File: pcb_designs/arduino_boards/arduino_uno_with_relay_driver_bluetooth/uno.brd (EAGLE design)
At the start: 96.2 x 69.8 mm, 27 parts, among them IC1 ATMEGA328, IC2 7805, Q1 12MHZ

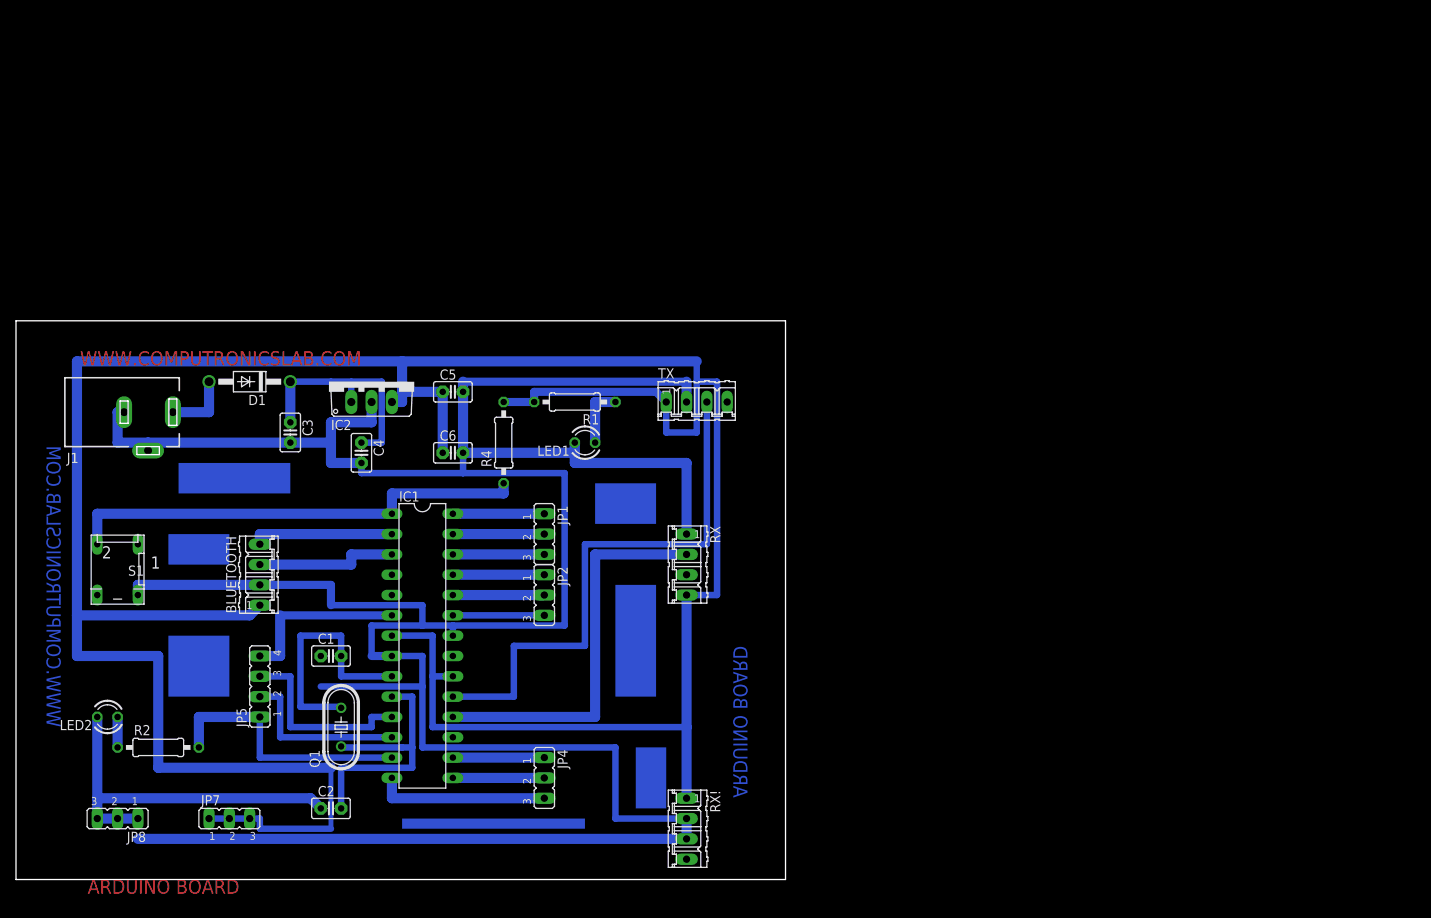
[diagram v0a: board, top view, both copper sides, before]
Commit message: 
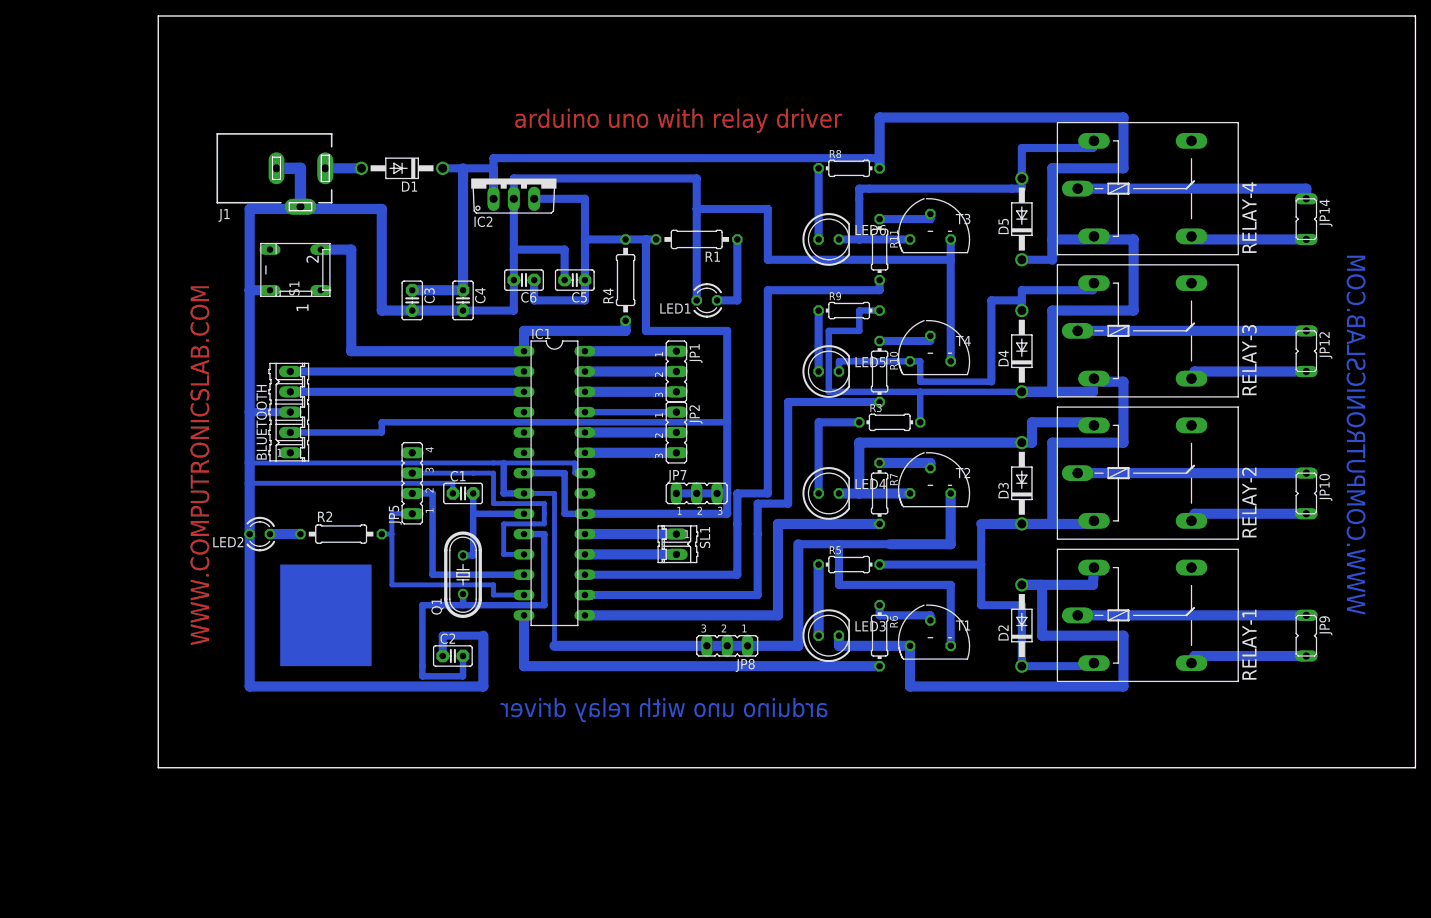
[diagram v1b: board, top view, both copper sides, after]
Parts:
- removed JP4: (no value), jumper:JP2
- removed RX, RX!, TX: (no value), con-amp-quick:04P
- added D2, D3, D4, D5: 1N4007, diode:DO41-10
- added JP10, JP12, JP14, JP9: AC CONNECTOR, jumper:JP1
- added LED3, LED4, LED5, LED6: 5MM, led:LED5MM
- added R10, R11, R6, R7: 5.6K, rcl:0204/7
- added R3, R5, R8, R9: 1K, rcl:0204/7
- added RELAY-1, RELAY-2, RELAY-3, RELAY-4: 12V, relay:G5LE
- added SL1: (no value), con-amp-quick:02P
- added T1, T2, T3, T4: BC547, transistor:TO92
- BLUETOOTH: value (none) -> 5 pin; device con-amp-quick:04P -> con-amp-quick:05P
- C3: value 470UF -> 100UF
- moved JP8 79.2 mm to (74.9, 24.1)
- moved JP7 71.2 mm to (71.1, 43.2)
- moved S1 43.3 mm to (21.6, 71.1), turned to 90 degrees
- moved J1 35.9 mm to (21.6, 83.8)
- moved R2 35.1 mm to (26.7, 38.1)
- moved D1 32.8 mm to (34.3, 83.8)
- moved JP5 31.8 mm to (35.6, 44.5)
- moved IC2 31.0 mm to (48.3, 82.5)
- moved LED2 29.8 mm to (16.5, 38.1)
- moved IC1 26.2 mm to (53.3, 44.5)
- moved C1 26.2 mm to (41.9, 43.2)
- moved JP1 26.2 mm to (68.6, 58.4)
- moved JP2 26.2 mm to (68.6, 50.8)
- moved R1 25.4 mm to (71.1, 74.9)
- moved R4 25.4 mm to (62.2, 69.8)
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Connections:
- removed net N$17: BLUETOOTH.3, IC1.3
- removed net N$18: IC1.6, JP5.4
- removed net N$22: IC1.14, JP4.3
- removed net N$23: IC1.15, JP4.2
- removed net N$24: IC1.16, JP4.1
- removed net N$26: IC1.18, RX.2
- new net N$16: BLUETOOTH.4, IC1.3
- new net N$28: D2.A, LED3.K, RELAY-1.2, T1.3
- new net N$29: R7.1, T2.2
- new net N$30: R6.1, T1.2
- new net N$33: LED3.A, R5.1
- new net N$34: LED4.A, R3.1
- new net N$35: JP9.2, RELAY-1.S
- new net N$36: JP9.1, RELAY-1.P
- new net N$38: JP10.2, RELAY-2.S
- new net N$39: JP10.1, RELAY-2.P
- new net N$41: IC1.14, R6.2
- new net N$42: D3.A, LED4.K, RELAY-2.2, T2.3
- new net N$43: D4.A, LED5.K, RELAY-3.2, T4.3
- new net N$45: R11.1, T3.2
- new net N$46: R10.1, T4.2
- new net N$47: LED5.A, R9.1
- new net N$48: LED6.A, R8.1
- new net N$49: JP12.2, RELAY-3.S
- new net N$50: JP12.1, RELAY-3.P
- new net N$51: JP14.2, RELAY-4.S
- new net N$53: JP14.1, RELAY-4.P
- new net N$55: BLUETOOTH.3, C1.1, C2.1, C3.2, C4.2, C5.2, C6.2, IC1.22, IC1.8, IC2.2, J1.2, J1.3, JP8.1, JP8.2, JP8.3, LED1.K, LED2.K, S1.4, T1.1, T2.1, T3.1, T4.1
- new net N$56: IC1.16, R10.2
- new net N$57: IC1.17, R11.2
- new net N$58: D5.A, LED6.K, RELAY-4.2, T3.3
- new net N$59: IC1.15, R7.2
- net N$14: now also JP5.4; no longer BLUETOOTH.4, IC1.2
- net N$15: now also BLUETOOTH.5, IC1.2; no longer S1.3
- net N$27: now also SL1.1; no longer TX.3
- net N$4: now also BLUETOOTH.2; no longer BLUETOOTH.1, RX!.1, RX.4, TX.1
- net N$5: now also IC1.18, SL1.2; no longer BLUETOOTH.2, C1.1, C2.1, C3.2, C4.2, C5.2, C6.2, IC1.22, IC1.8, IC2.2, J1.2, J1.3, JP8.1, JP8.2, JP8.3, LED1.K, LED2.K, RX!.2, RX!.3, RX.1, S1.4, TX.2
- net N$7: now also D2.C, D3.C, D4.C, D5.C, R3.2, R5.2, R8.2, R9.2, RELAY-1.1, RELAY-2.1, RELAY-3.1, RELAY-4.1
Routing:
- net N$55: track 0.00 -> 478.3 mm
- net N$5: track 436.7 -> 11.4 mm
- net N$7: track 31.7 -> 341.8 mm
- net N$4: track 374.4 -> 179.1 mm
- net N$28: track 0.00 -> 78.4 mm
- net N$57: track 0.00 -> 73.7 mm
- net N$56: track 0.00 -> 61.0 mm
- net N$27: track 68.6 -> 11.4 mm
- net N$41: track 0.00 -> 50.8 mm
- net N$58: track 0.00 -> 50.4 mm
- net N$26: track 49.5 -> 0.00 mm
- net N$43: track 0.00 -> 49.2 mm
- net N$59: track 0.00 -> 48.3 mm
- net N$42: track 0.00 -> 47.4 mm
- net N$53: track 0.00 -> 29.8 mm
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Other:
- board size 96.2 x 69.8 mm -> 157.2 x 94 mm
- board text added: "arduino uno with relay driver"
- board text removed: "ARDUINO BOARD"
